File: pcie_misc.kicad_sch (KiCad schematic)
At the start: 33 parts, among them U37 9DBL0651CKILF, U38 74AUP2G132, Y1 Oscillator_32.768kHz_ECS_2520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

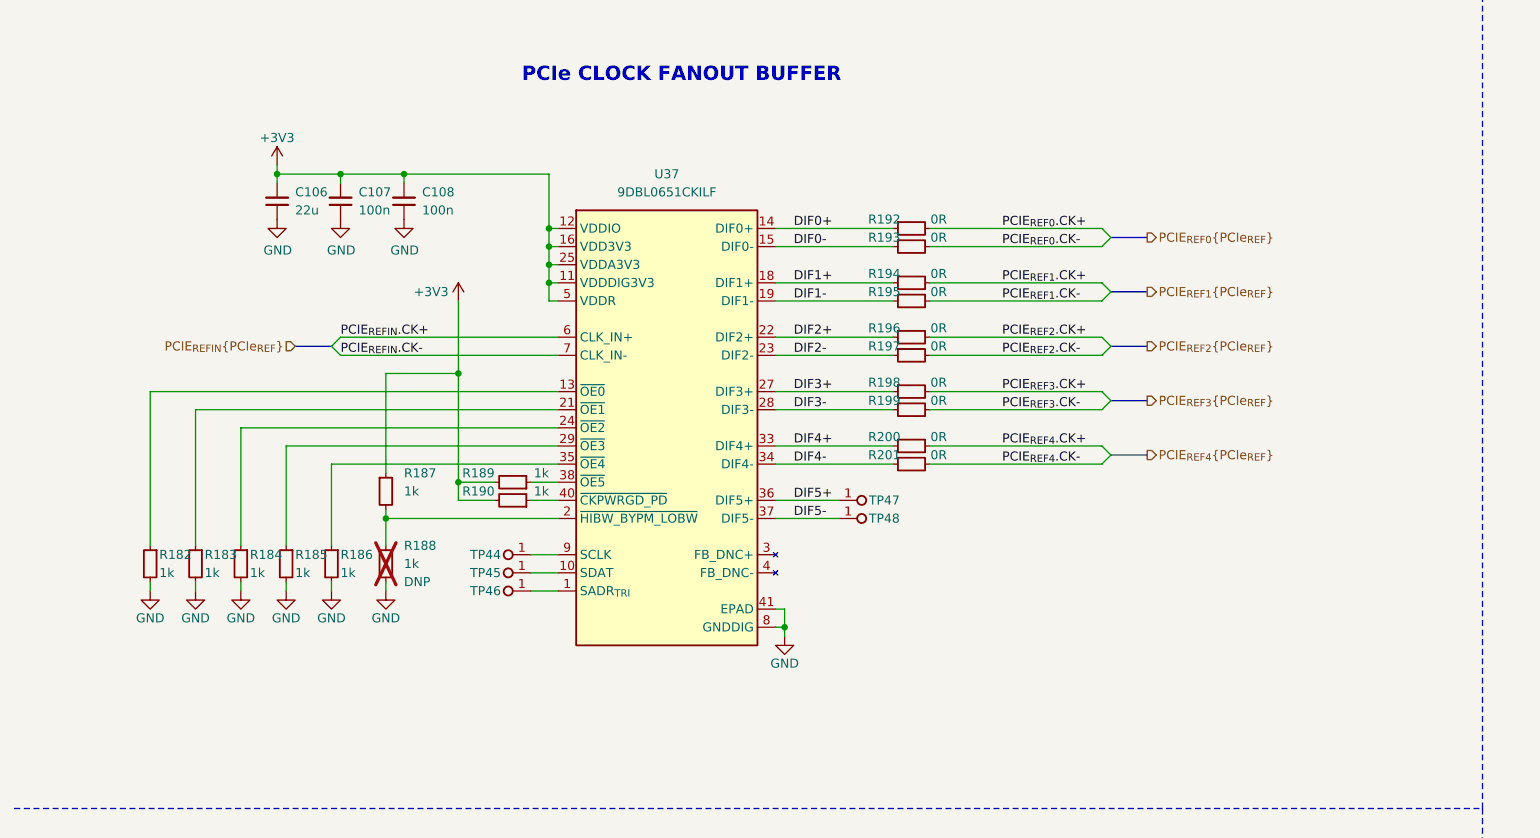
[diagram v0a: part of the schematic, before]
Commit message: [#58904] Change pinout of backplane connector. Connect CLKREQ from PCIe devices
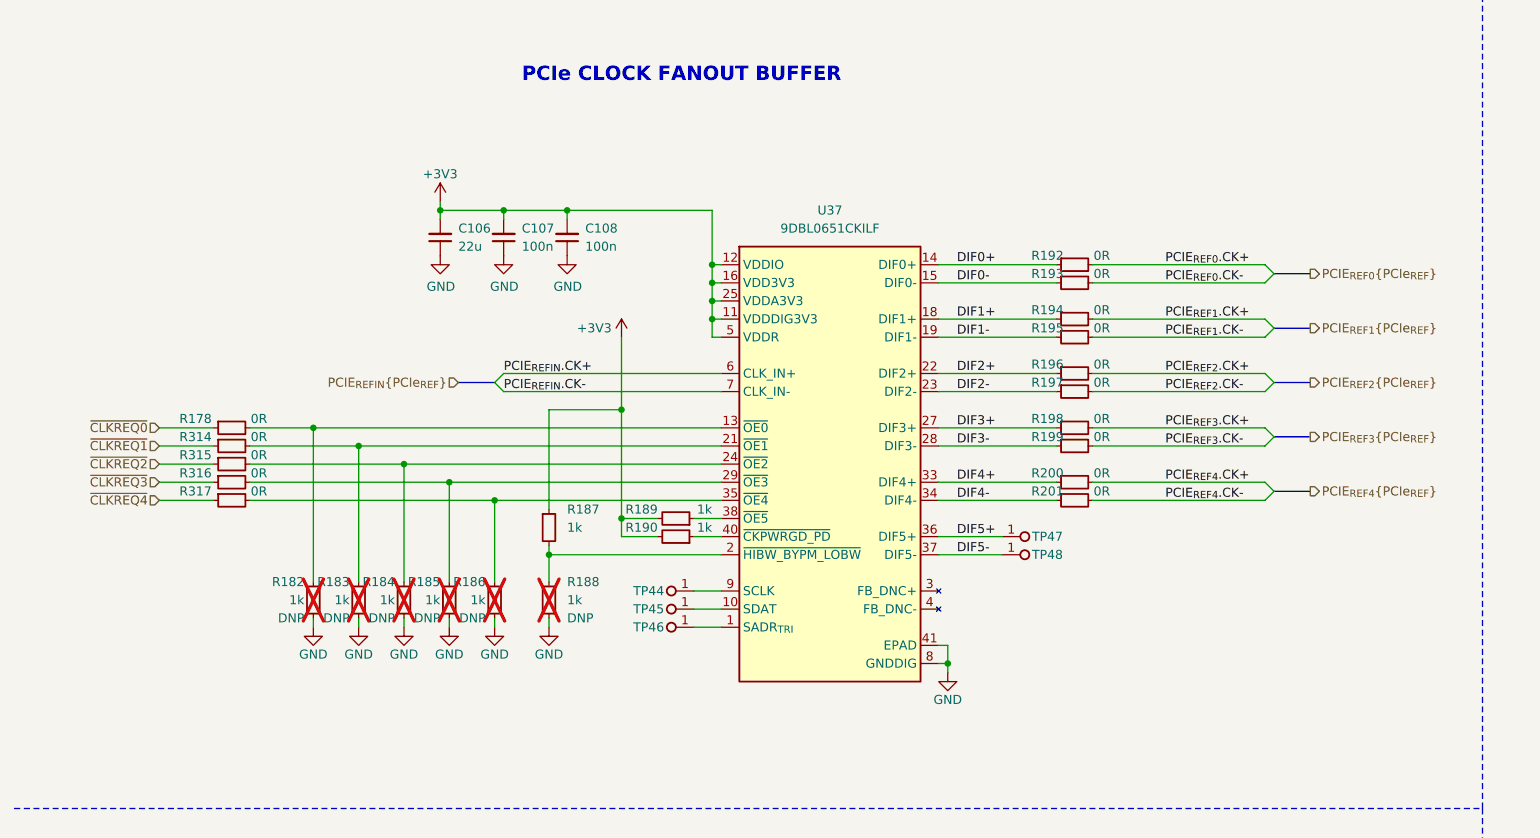
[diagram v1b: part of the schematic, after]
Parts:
- added R178, R314, R315, R316, R317: R_0R_0402, antmicro-footprints:R_0402_1005Metric, symbol antmicroResistors0402:R_0R_0402
- R182, R183, R184, R185, R186: DNP (none) -> DNP; now not fitted
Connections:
- net at R182.1, U37.13 (~{OE0}): now also R178.2
- net at R185.1, U37.29 (~{OE3}): now also R316.2
- net at R183.1, U37.21 (~{OE1}): now also R314.2
- net at R184.1, U37.24 (~{OE2}): now also R315.2
- net at R186.1, U37.35 (~{OE4}): now also R317.2
- new net ~{CLKREQ0}: R178.1
- new net ~{CLKREQ1}: R314.1
- new net ~{CLKREQ2}: R315.1
- new net ~{CLKREQ3}: R316.1
- new net ~{CLKREQ4}: R317.1
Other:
- moved on the sheet: C106, C107, C108, R187, R188, R189, R190, R192, R193, R194, R195, R196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

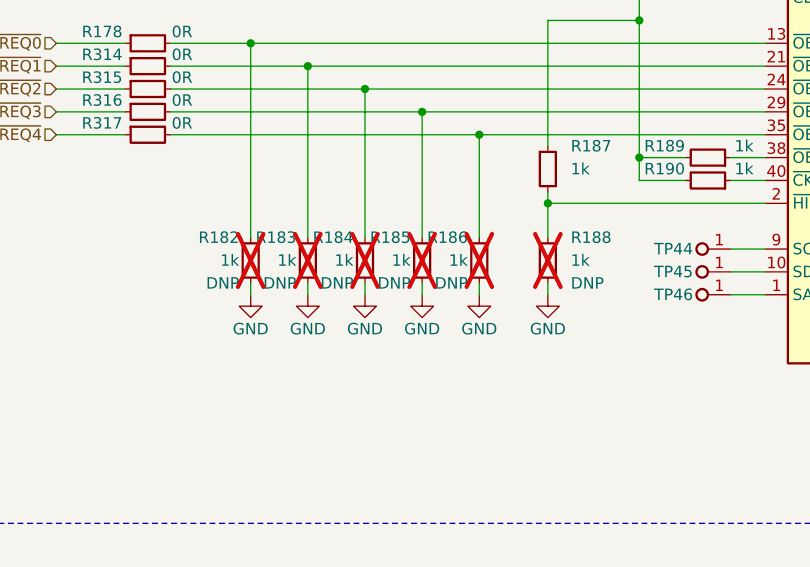
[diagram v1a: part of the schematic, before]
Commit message: Update components from the library
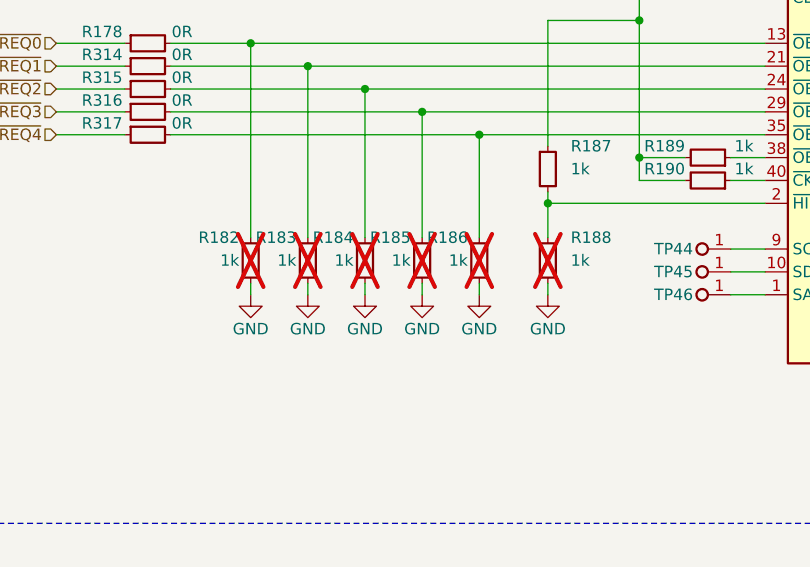
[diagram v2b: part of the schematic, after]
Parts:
- C106, C107, C108, C109, C110, R178, R187, R189, R190, R191, R192, R193, R194, R195, R196, R197, R198, R199, R200, R201, R314, R315, R316, R317, TP44, TP45, TP46, TP47, TP48: Public (none) -> False
- R182, R183, R184, R185, R186, R188: DNP DNP -> (none); Public (none) -> False
- Y1: Public (none) -> False; now in the parts list

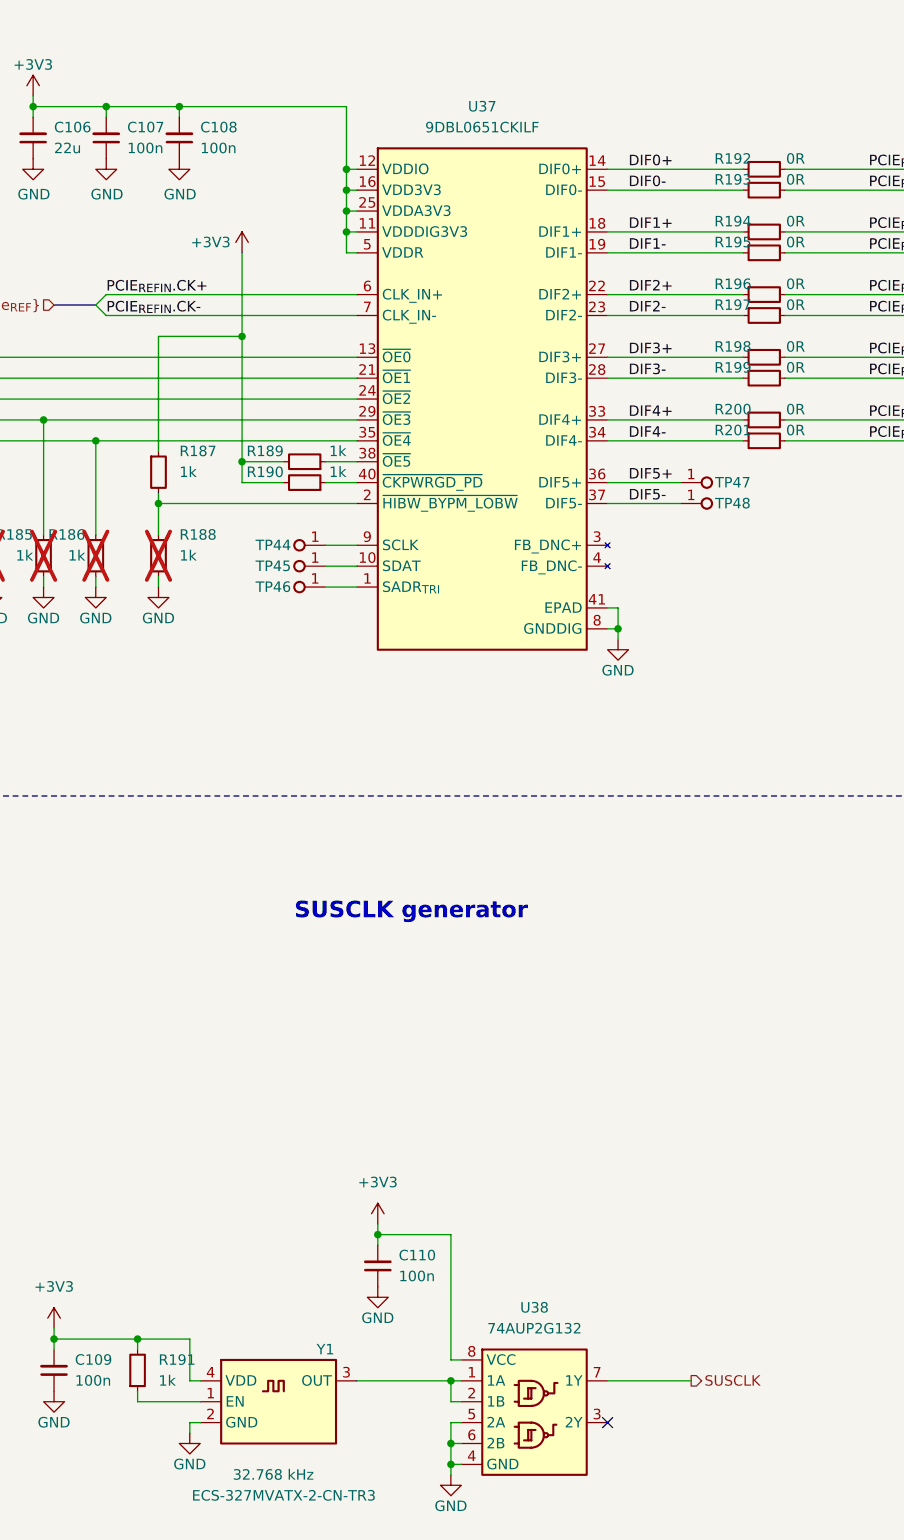
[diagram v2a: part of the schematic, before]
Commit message: [#65447] Fix rotated LEDs, overlapping text and symbols, add rules
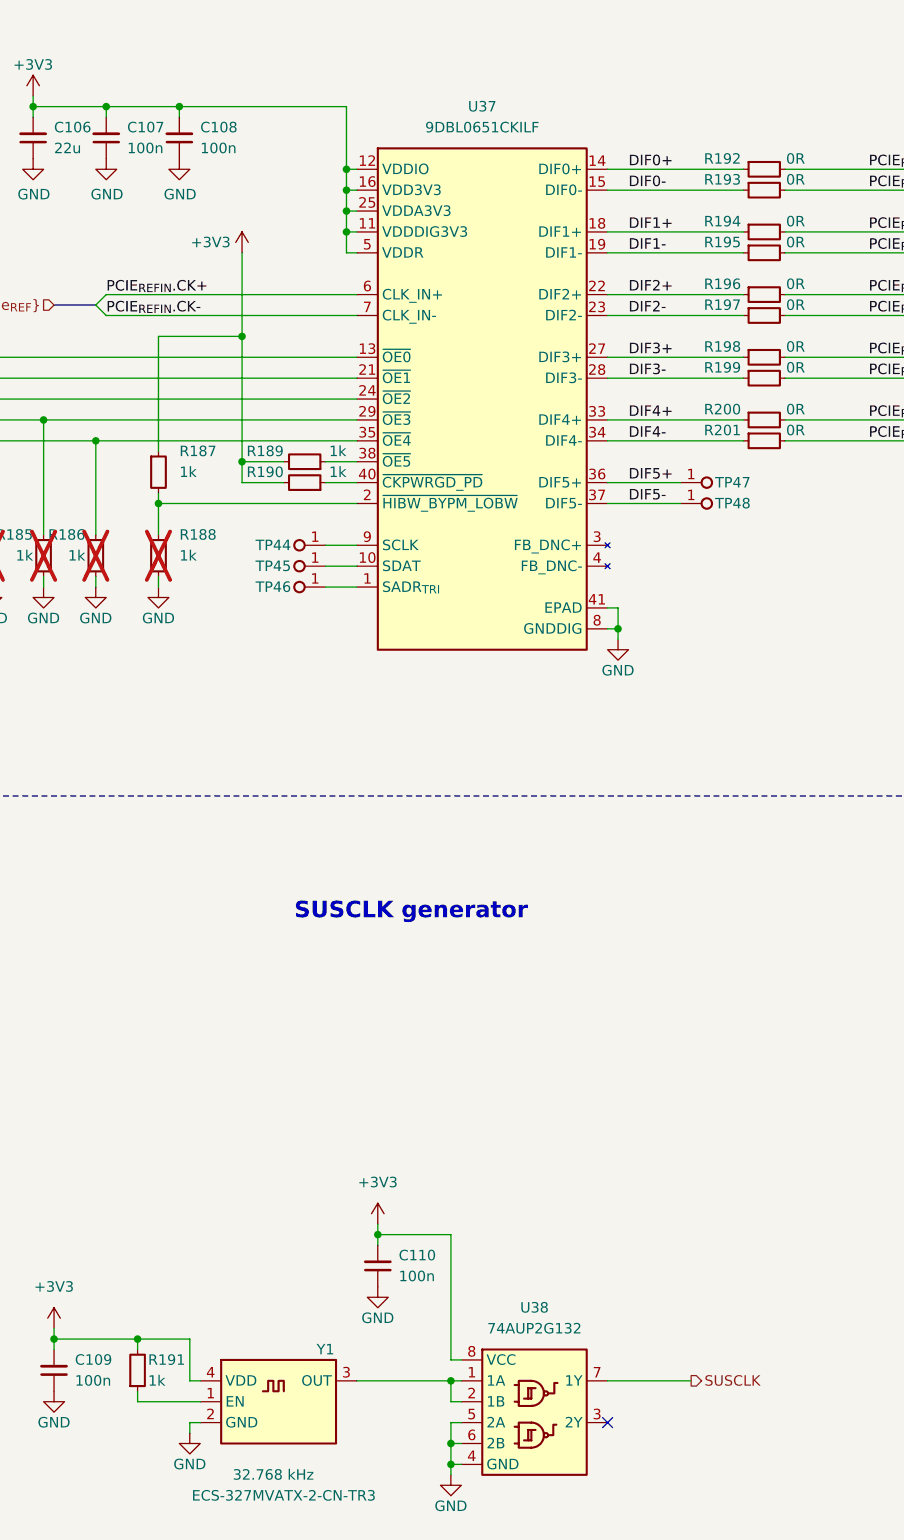
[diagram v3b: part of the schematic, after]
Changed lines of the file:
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@@
   (symbol (lib_id "antmicroResistors0402:R_0R_0402") (at 158.75 73.66 0) (unit 1)
     (in_bom yes) (on_board yes) (dnp no)
-    (property "Reference" "R196" (at 157.48 72.39 0)
+    (property "Reference" "R196" (at 156.21 72.39 0)
       (effects (font (size 1.27 1.27) (thickness 0.15)))
     )
@@
   )
   (symbol (lib_id "antmicroResistors0402:R_1k_0402") (at 85.09 207.01 90) (unit 1)
-    (in_bom yes) (on_board yes) (dnp no) (fields_autoplaced)
-    (property "Reference" "R191" (at 87.63 203.2 90)
+    (in_bom yes) (on_board yes) (dnp no)
+    (property "Reference" "R191" (at 86.36 203.2 90)
       (effects (font (size 1.27 1.27) (thickness 0.15)) (justify right))
     )
@@
       (effects (font (size 1.27 1.27) (thickness 0.15)) (justify left bottom) hide)
     )
-    (property "Val" "1k" (at 87.63 205.74 90)
+    (property "Val" "1k" (at 86.36 205.74 90)
       (effects (font (size 1.27 1.27) (thickness 0.15)) (justify right))
     )
@@
   (symbol (lib_id "antmicroResistors0402:R_0R_0402") (at 158.75 68.58 0) (unit 1)
     (in_bom yes) (on_board yes) (dnp no)
-    (property "Reference" "R195" (at 157.48 67.31 0)
+    (property "Reference" "R195" (at 156.21 67.31 0)
       (effects (font (size 1.27 1.27) (thickness 0.15)))
     )
@@
   (symbol (lib_id "antmicroResistors0402:R_0R_0402") (at 158.75 88.9 0) (unit 1)
     (in_bom yes) (on_board yes) (dnp no)
-    (property "Reference" "R200" (at 157.48 87.63 0)
+    (property "Reference" "R200" (at 156.21 87.63 0)
       (effects (font (size 1.27 1.27) (thickness 0.15)))
     )
@@
   (symbol (lib_id "antmicroResistors0402:R_0R_0402") (at 158.75 83.82 0) (unit 1)
     (in_bom yes) (on_board yes) (dnp no)
-    (property "Reference" "R199" (at 157.48 82.55 0)
+    (property "Reference" "R199" (at 156.21 82.55 0)
       (effects (font (size 1.27 1.27) (thickness 0.15)))
     )
@@
   (symbol (lib_id "antmicroResistors0402:R_0R_0402") (at 158.75 58.42 0) (unit 1)
     (in_bom yes) (on_board yes) (dnp no)
-    (property "Reference" "R192" (at 157.48 57.15 0)
+    (property "Reference" "R192" (at 156.21 57.15 0)
       (effects (font (size 1.27 1.27) (thickness 0.15)))
     )
@@
   (symbol (lib_id "antmicroResistors0402:R_0R_0402") (at 158.75 91.44 0) (unit 1)
     (in_bom yes) (on_board yes) (dnp no)
-    (property "Reference" "R201" (at 157.48 90.17 0)
+    (property "Reference" "R201" (at 156.21 90.17 0)
       (effects (font (size 1.27 1.27) (thickness 0.15)))
     )
@@
   (symbol (lib_id "antmicroResistors0402:R_0R_0402") (at 158.75 81.28 0) (unit 1)
     (in_bom yes) (on_board yes) (dnp no)
-    (property "Reference" "R198" (at 157.48 80.01 0)
+    (property "Reference" "R198" (at 156.21 80.01 0)
       (effects (font (size 1.27 1.27) (thickness 0.15)))
     )
@@
   (symbol (lib_id "antmicroResistors0402:R_0R_0402") (at 158.75 76.2 0) (unit 1)
     (in_bom yes) (on_board yes) (dnp no)
-    (property "Reference" "R197" (at 157.48 74.93 0)
+    (property "Reference" "R197" (at 156.21 74.93 0)
       (effects (font (size 1.27 1.27) (thickness 0.15)))
     )
@@
   (symbol (lib_id "antmicroResistors0402:R_0R_0402") (at 158.75 66.04 0) (unit 1)
     (in_bom yes) (on_board yes) (dnp no)
-    (property "Reference" "R194" (at 157.48 64.77 0)
+    (property "Reference" "R194" (at 156.21 64.77 0)
       (effects (font (size 1.27 1.27) (thickness 0.15)))
     )
@@
   (symbol (lib_id "antmicroResistors0402:R_0R_0402") (at 158.75 60.96 0) (unit 1)
     (in_bom yes) (on_board yes) (dnp no)
-    (property "Reference" "R193" (at 157.48 59.69 0)
-      (effects (font (size 1.27 1.27) (thickness 0.15)))
-    )
+    (property "Reference" "R193" (at 156.21 59.69 0)
+      (effects (font (size 1.27 1.27) (thickness 0.15)))
+    )
